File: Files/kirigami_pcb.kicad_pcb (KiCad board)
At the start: 2 copper layers, 67.7 x 70.4 mm, 24 parts, among them J1 In, J2 Thermistor, J3 Heater, J4 Fuse, J5 Fan, J6 Neopixel

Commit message: chain order
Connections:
- D1 pad 4: /DataOut -> Net-(D1-DIN)
- D8 pad 2: Net-(D8-DOUT) -> /DataIn
- J1 pad 3: Net-(D8-DOUT) -> /DataOut
- J1 pad 4: /DataIn -> Net-(D1-DIN)
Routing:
- net Net-(D8-DOUT): track 43.8 -> 0.00 mm, vias 1 -> 0
- net Net-(D1-DIN): track 0.00 -> 38.3 mm
- net /DataIn: track 21.1 -> 50.4 mm, vias 0 -> 1
- net /DataOut: track 20.9 -> 25.3 mm
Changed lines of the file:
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@@
   (net 15 "Net-(D6-DOUT)")
   (net 16 "Net-(D7-DOUT)")
-  (net 17 "Net-(D8-DOUT)")
+  (net 17 "Net-(D1-DIN)")
   (net 18 "Net-(D4-DOUT)")
   (net 19 "Net-(D5-DOUT)")
@@
       (net 10 "/Thermistor-Pad2") (pinfunction "Pin_2") (pintype "passive"))
     (pad "3" thru_hole circle (at 6 0 180) (size 1.5 1.5) (drill 1.02) (layers "*.Cu" "*.Mask")
-      (net 17 "Net-(D8-DOUT)") (pinfunction "Pin_3") (pintype "passive"))
+      (net 8 "/DataOut") (pinfunction "Pin_3") (pintype "passive"))
     (pad "4" thru_hole circle (at 9 0 180) (size 1.5 1.5) (drill 1.02) (layers "*.Cu" "*.Mask")
-      (net 7 "/DataIn") (pinfunction "Pin_4") (pintype "passive"))
+      (net 17 "Net-(D1-DIN)") (pinfunction "Pin_4") (pintype "passive"))
     (pad "5" thru_hole circle (at 12 0 180) (size 1.5 1.5) (drill 1.02) (layers "*.Cu" "*.Mask")
       (net 9 "/Neopixel5v") (pinfunction "Pin_5") (pintype "passive"))
@@
       (net 9 "/Neopixel5v") (pinfunction "VDD") (pintype "power_in"))
     (pad "2" smd rect (at -2.45 -1.65 200) (size 1.5 0.9) (layers "B.Cu" "B.Paste" "B.Mask")
-      (net 17 "Net-(D8-DOUT)") (pinfunction "DOUT") (pintype "output"))
+      (net 7 "/DataIn") (pinfunction "DOUT") (pintype "output"))
     (pad "3" smd rect (at 2.45 -1.65 200) (size 1.5 0.9) (layers "B.Cu" "B.Paste" "B.Mask")
       (net 6 "/NeopixelGND") (pinfunction "VSS") (pintype "power_in"))
@@
       (net 6 "/NeopixelGND") (pinfunction "VSS") (pintype "power_in"))
     (pad "4" smd rect (at 2.45 1.65 340) (size 1.5 0.9) (layers "B.Cu" "B.Paste" "B.Mask")
-      (net 8 "/DataOut") (pinfunction "DIN") (pintype "input"))
+      (net 17 "Net-(D1-DIN)") (pinfunction "DIN") (pintype "input"))
     (model "${KICAD6_3DMODEL_DIR}/LED_SMD.3dshapes/LED_WS2812B_PLCC4_5.0x5.0mm_P3.2mm.wrl"
       (offset (xyz 0 0 0))
@@
   (segment (start 199.025 67.175) (end 199.025 41.805645) (width 0.5) (layer "B.Cu") (net 6))
   (segment (start 180.875216 56.158867) (end 180.330141 56.158267) (width 0.5) (layer "B.Cu") (net 6))
-  (segment (start 203.8064 71.0036) (end 201.5011 71.0036) (width 0.5) (layer "B.Cu") (net 7))
-  (segment (start 211.1974 63.6126) (end 203.8064 71.0036) (width 0.5) (layer "B.Cu") (net 7))
-  (segment (start 219.0011 62.2336) (end 217.6221 63.6126) (width 0.5) (layer "B.Cu") (net 7))
-  (segment (start 217.6221 63.6126) (end 211.1974 63.6126) (width 0.5) (layer "B.Cu") (net 7))
-  (segment (start 203.95 75.95) (end 203.95 87.1) (width 0.5) (layer "B.Cu") (net 8))
-  (segment (start 201.60573 73.60573) (end 203.95 75.95) (width 0.5) (layer "B.Cu") (net 8))
-  (segment (start 199.684773 91.365227) (end 199.684773 91.790227) (width 0.5) (layer "B.Cu") (net 8))
-  (segment (start 203.95 87.1) (end 199.684773 91.365227) (width 0.5) (layer "B.Cu") (net 8))
+  (segment (start 205.8853 71) (end 201.5 71) (width 0.5) (layer "F.Cu") (net 7))
+  (segment (start 214.075 62.8103) (end 205.8853 71) (width 0.5) (layer "F.Cu") (net 7))
+  (segment (start 214.075 40.625) (end 214.075 62.8103) (width 0.5) (layer "F.Cu") (net 7))
+  (via (at 214.075 40.625) (size 0.6) (drill 0.3) (layers "F.Cu" "B.Cu") (net 7))
+  (segment (start 222.715254 31.984746) (end 214.075 40.625) (width 0.5) (layer "B.Cu") (net 7))
+  (segment (start 220.2 63.8) (end 222 62) (width 0.5) (layer "F.Cu") (net 8))
+  (segment (start 201.5 73.5) (end 205.9 73.5) (width 0.5) (layer "F.Cu") (net 8))
+  (segment (start 215.6 63.8) (end 220.2 63.8) (width 0.5) (layer "F.Cu") (net 8))
+  (segment (start 205.9 73.5) (end 215.6 63.8) (width 0.5) (layer "F.Cu") (net 8))
   (segment (start 208.5575 62) (end 208.0011 61.4436) (width 0.5) (layer "F.Cu") (net 9))
   (segment (start 210.4925 62) (end 208.5575 62) (width 0.5) (layer "F.Cu") (net 9))
@@
   (segment (start 200.472523 40.075) (end 207.514277 40.075) (width 0.5) (layer "B.Cu") (net 16))
   (segment (start 207.514277 40.075) (end 217.029617 30.55966) (width 0.5) (layer "B.Cu") (net 16))
-  (segment (start 219.8347 64.175) (end 222.0011 62.0086) (width 0.5) (layer "F.Cu") (net 17))
-  (segment (start 215.4397 64.175) (end 219.8347 64.175) (width 0.5) (layer "F.Cu") (net 17))
-  (segment (start 214.075 40.625) (end 214.075 62.8103) (width 0.5) (layer "F.Cu") (net 17))
-  (segment (start 214.075 62.8103) (end 215.4397 64.175) (width 0.5) (layer "F.Cu") (net 17))
-  (via (at 214.075 40.625) (size 0.6) (drill 0.3) (layers "F.Cu" "B.Cu") (net 17))
-  (segment (start 222.715254 31.984746) (end 214.075 40.625) (width 0.5) (layer "B.Cu") (net 17))
+  (segment (start 199.684773 91.365227) (end 199.684773 91.790227) (width 0.5) (layer "B.Cu") (net 17))
+  (segment (start 217.6221 63.6126) (end 216.2874 63.6126) (width 0.5) (layer "B.Cu") (net 17))
+  (segment (start 216.2874 63.6126) (end 203.95 75.95) (width 0.5) (layer "B.Cu") (net 17))
+  (segment (start 219.0011 62.2336) (end 217.6221 63.6126) (width 0.5) (layer "B.Cu") (net 17))
+  (segment (start 203.95 87.1) (end 199.684773 91.365227) (width 0.5) (layer "B.Cu") (net 17))
+  (segment (start 203.95 75.95) (end 203.95 87.1) (width 0.5) (layer "B.Cu") (net 17))
   (segment (start 182.42266 62.85234) (end 182.206476 63.068524) (width 0.5) (layer "B.Cu") (net 18))
   (segment (start 182.206476 63.068524) (end 177.842116 63.068524) (width 0.5) (layer "B.Cu") (net 18))

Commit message: Update kirigami_pcb.kicad_pcb
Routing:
- net /Fan-: track 22.6 -> 23.6 mm
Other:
- board text added: "V0 Kirigami PCB V2 U.F.O. Edition 8/8/23 L. Ries JLCJLCJLCJLC"
- board text removed: "V0 Kirigami PCB V2 - 10/16/22 L. Ries JLCJLCJLCJLC"

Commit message: Update kirigami_pcb.kicad_pcb
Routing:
- net /Neopixel5v: track 266.1 -> 202.0 mm
- net /NeopixelGND: track 196.5 -> 176.9 mm
- net Net-(D3-DOUT): track 19.2 -> 7.99 mm
- net Net-(D2-DOUT): track 9.49 -> 10.8 mm

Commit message: Update kirigami_pcb.kicad_pcb
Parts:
- moved C1 2.86 mm to (210.6, 60.0)
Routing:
- net /Neopixel5v: track 202.0 -> 197.1 mm
- net /NeopixelGND: track 176.9 -> 174.2 mm
- net /DataIn: track 50.4 -> 48.8 mm
- net /Fan-: track 23.6 -> 22.3 mm
- net Net-(D5-DOUT): track 13.3 -> 12.7 mm

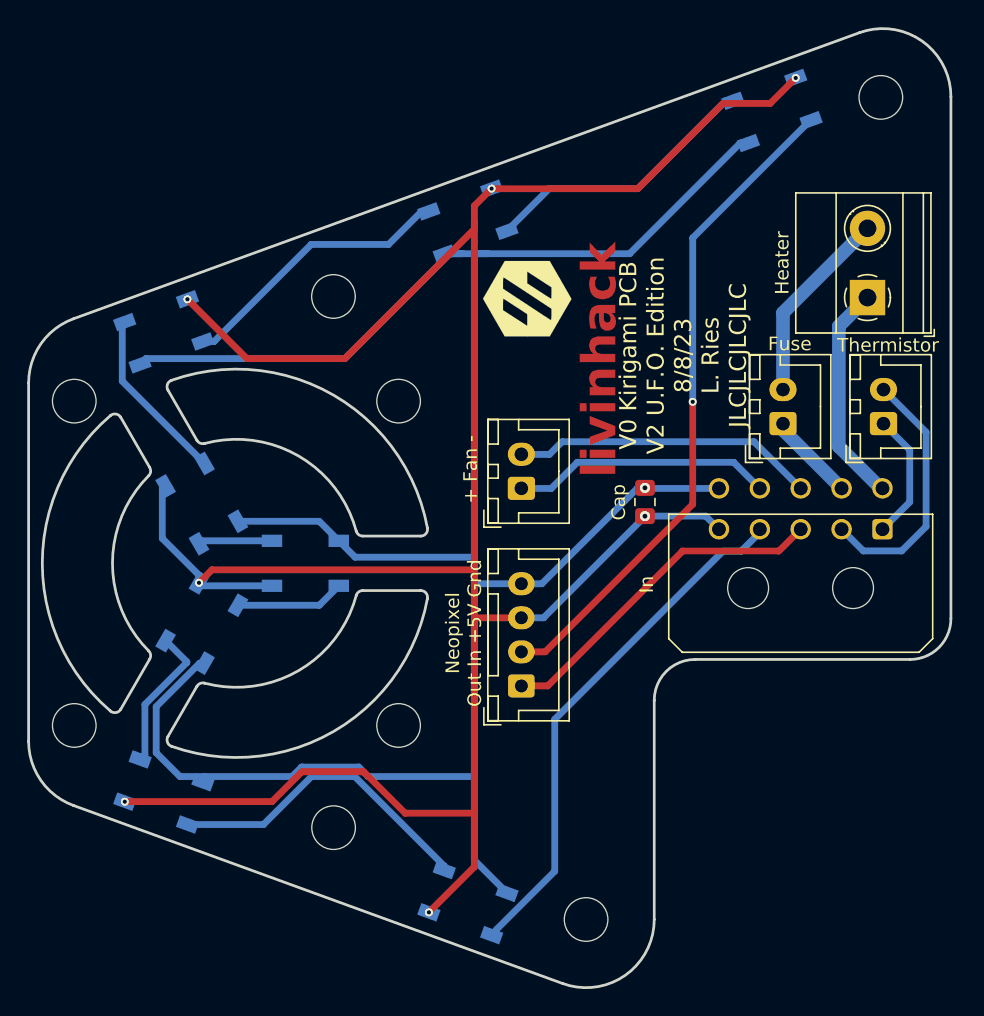
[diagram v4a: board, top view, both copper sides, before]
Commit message: round tracks
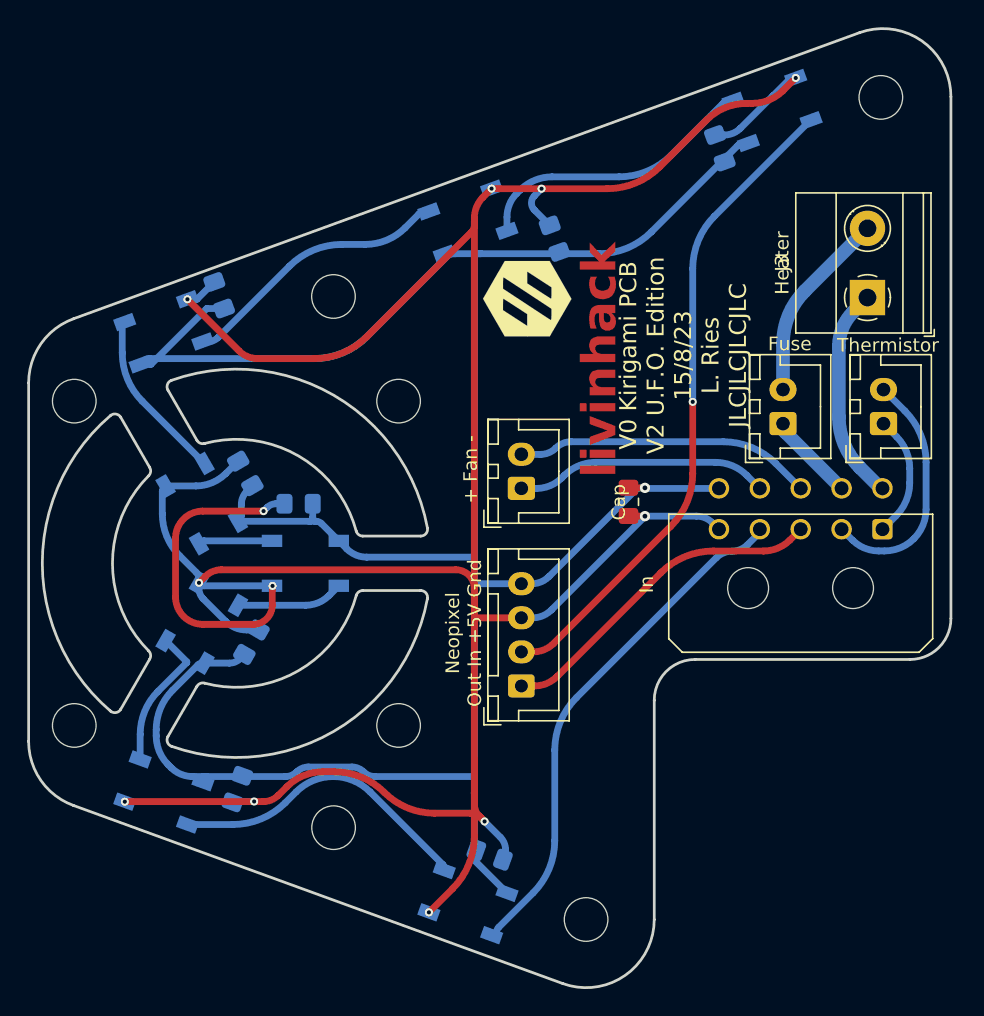
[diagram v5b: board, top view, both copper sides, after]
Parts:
- added C1: Cap, Capacitor_SMD:C_0805_2012Metric_Pad1.18x1.45mm_HandSolder, B.Cu at (199.2, 85.9)
- added C2: Cap, Capacitor_SMD:C_0805_2012Metric_Pad1.18x1.45mm_HandSolder, B.Cu at (180.7, 81.1)
- added C3: Cap, Capacitor_SMD:C_0805_2012Metric_Pad1.18x1.45mm_HandSolder, B.Cu at (181.7, 70.3)
- added C4: Cap, Capacitor_SMD:C_0805_2012Metric_Pad1.18x1.45mm_HandSolder, B.Cu at (185.2, 60.1)
- added C5: Cap, Capacitor_SMD:C_0805_2012Metric_Pad1.18x1.45mm_HandSolder, B.Cu at (181.2, 57.9)
- added C6: Cap, Capacitor_SMD:C_0805_2012Metric_Pad1.18x1.45mm_HandSolder, B.Cu at (179.3, 44.8)
- added C7: Cap, Capacitor_SMD:C_0805_2012Metric_Pad1.18x1.45mm_HandSolder, B.Cu at (203.9, 40.7)
- added C8: Cap, Capacitor_SMD:C_0805_2012Metric_Pad1.18x1.45mm_HandSolder, B.Cu at (216.1, 34.0)
- moved C9 1.21 mm to (209.4, 60.0), turned to -90 degrees
- renumbered C1 to C9
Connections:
- C9 pad 1: /Neopixel5v -> /NeopixelGND
- C9 pad 2: /NeopixelGND -> /Neopixel5v
- D1 pad 2: Net-(D1-DOUT) -> Dout>Din
- D1 pad 4: Net-(D1-DIN) -> /DataIn
- D2 pad 2: Net-(D2-DOUT) -> Dout>Din
- D2 pad 4: Net-(D1-DOUT) -> Dout>Din
- D3 pad 2: Net-(D3-DOUT) -> Dout>Din
- D3 pad 4: Net-(D2-DOUT) -> Dout>Din
- D4 pad 2: Net-(D4-DOUT) -> Dout>Din
- D4 pad 4: Net-(D3-DOUT) -> Dout>Din
- D5 pad 2: Net-(D5-DOUT) -> Dout>Din
- D5 pad 4: Net-(D4-DOUT) -> Dout>Din
- D6 pad 2: Net-(D6-DOUT) -> Dout>Din
- D6 pad 4: Net-(D5-DOUT) -> Dout>Din
- D7 pad 2: Net-(D7-DOUT) -> Dout>Din
- D7 pad 4: Net-(D6-DOUT) -> Dout>Din
- D8 pad 2: /DataIn -> Dout>Din
- D8 pad 4: Net-(D7-DOUT) -> Dout>Din
- J1 pad 4: Net-(D1-DIN) -> /DataIn
- J6 pad 2: /DataIn -> Dout>Din
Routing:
- net Dout>Din: track 0.00 -> 147.1 mm, vias 0 -> 1
- net /Neopixel5v: track 197.1 -> 252.8 mm, vias 7 -> 12
- net Net-(D1-DIN): track 38.3 -> 0.00 mm
- net Net-(D1-DOUT): track 23.3 -> 0.00 mm
- net Net-(D6-DOUT): track 20.5 -> 0.00 mm
- net Net-(D7-DOUT): track 20.1 -> 0.00 mm
- net /NeopixelGND: track 174.2 -> 187.8 mm
- net Net-(D5-DOUT): track 12.7 -> 0.00 mm
- net /DataIn: track 48.8 -> 37.6 mm, vias 1 -> 0
- net Net-(D2-DOUT): track 10.8 -> 0.00 mm
- net Net-(D3-DOUT): track 7.99 -> 0.00 mm
- net Net-(D4-DOUT): track 5.45 -> 0.00 mm
- net /Thermistor-Pad2: track 19.0 -> 18.3 mm
- net /DataOut: track 25.3 -> 24.8 mm
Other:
- board text added: "V0 Kirigami PCB V2 U.F.O. Edition 15/8/23 L. Ries JLCJLCJLCJLC"
- board text removed: "V0 Kirigami PCB V2 U.F.O. Edition 8/8/23 L. Ries JLCJLCJLCJLC"

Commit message: Update kirigami_pcb.kicad_pcb
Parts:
- moved C9 1.21 mm to (210.6, 60.0)
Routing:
- net /Neopixel5v: track 252.8 -> 256.1 mm
- net /NeopixelGND: track 187.8 -> 186.9 mm

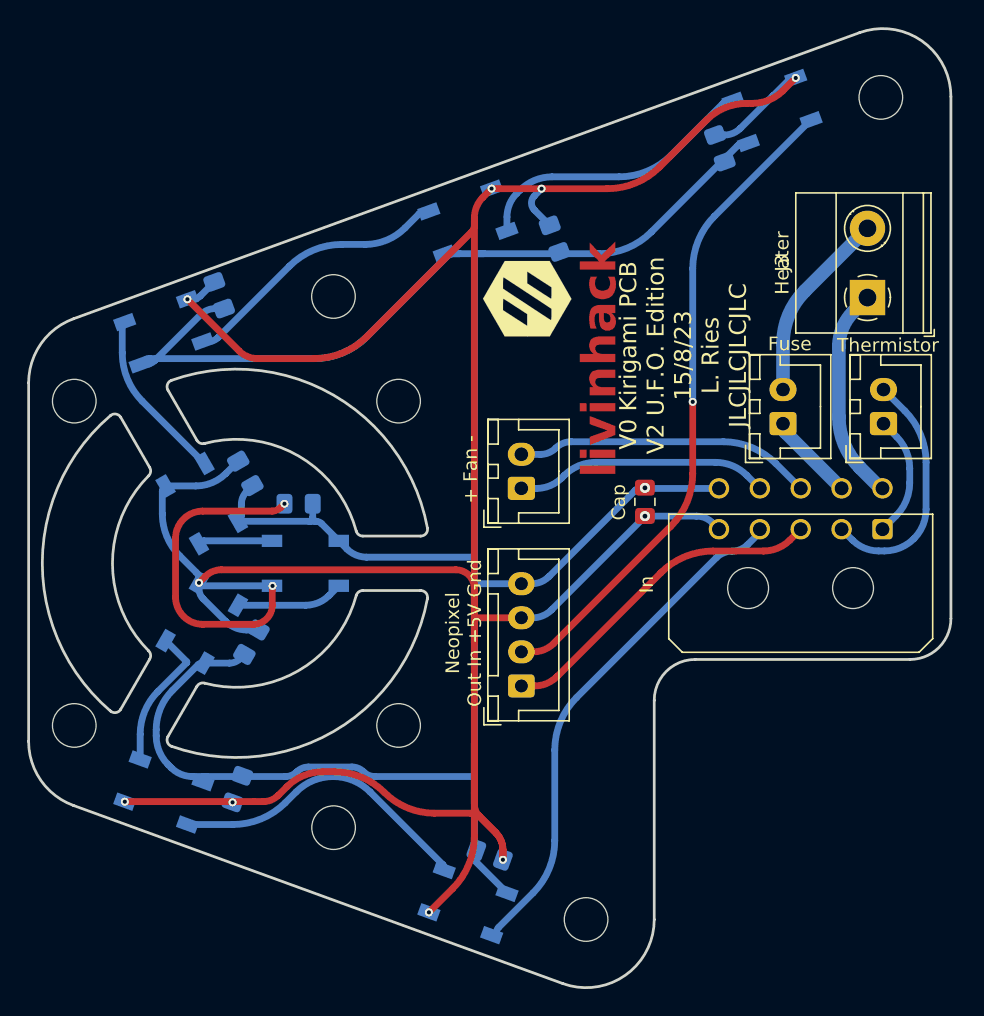
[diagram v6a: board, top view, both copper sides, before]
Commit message: Schematic cleanup and organization
A few changes to the schematic to aid in readability as well as simplifying signal flow.
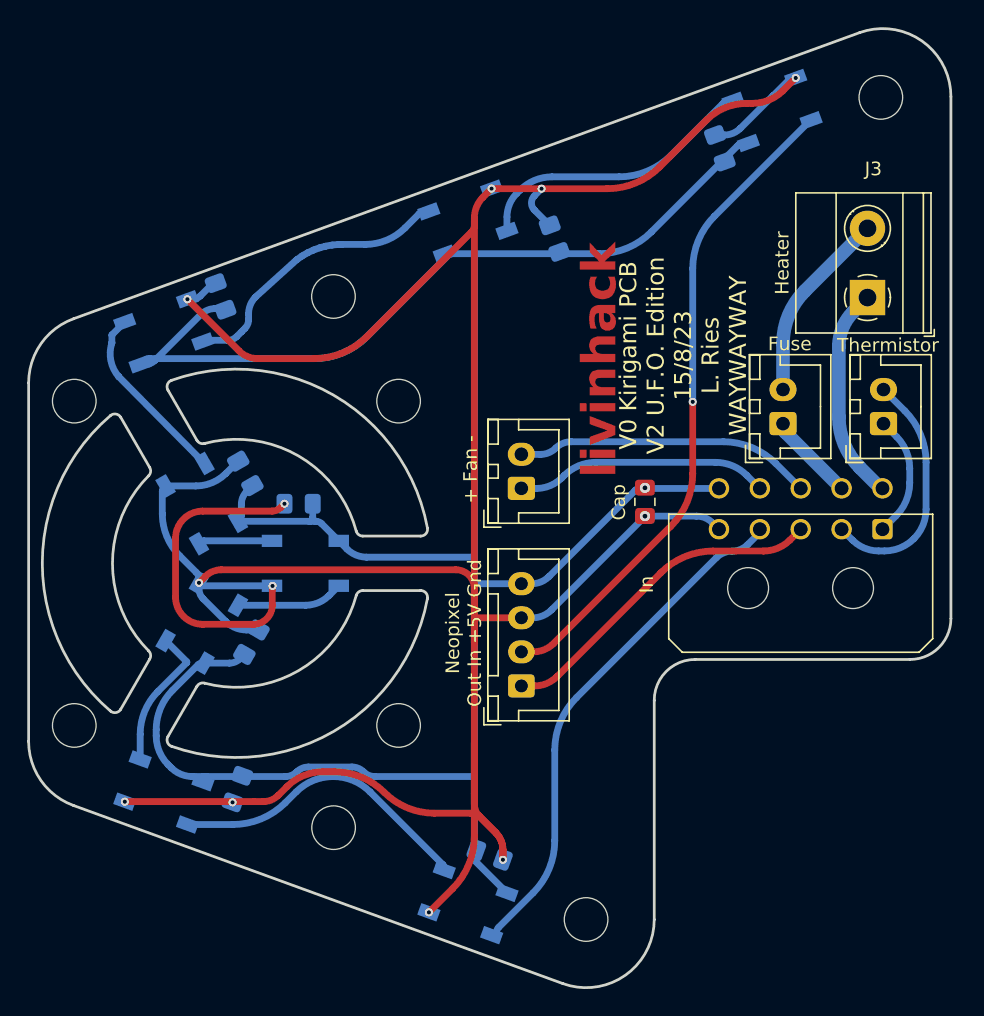
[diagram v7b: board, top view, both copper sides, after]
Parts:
- removed G***: LOGO, TRA_KiCad_Footprints:VoronLogo_6pt5mm_silkScreen
- J6: value Neopixel -> Front Neopixel
- moved C6 0.14 mm to (179.4, 44.9), turned to -70 degrees
- turned C1 to 160 degrees
- turned C2 to 70 degrees
- turned C3 to -120 degrees
- turned C4 to 0 degrees
- turned C5 to -60 degrees
- turned C7 to -70 degrees
- turned C8 to -70 degrees
- turned C9 to 90 degrees
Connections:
- net /DataIn renamed /Neo_In
- net /DataOut renamed /Neopixel Return
- C1 pad 1: /NeopixelGND -> /Neopixel5v
- C1 pad 2: /Neopixel5v -> /NeopixelGND
- C2 pad 1: /NeopixelGND -> /Neopixel5v
- C2 pad 2: /Neopixel5v -> /NeopixelGND
- C3 pad 1: /NeopixelGND -> /Neopixel5v
- C3 pad 2: /Neopixel5v -> /NeopixelGND
- C4 pad 1: /NeopixelGND -> /Neopixel5v
- C4 pad 2: /Neopixel5v -> /NeopixelGND
- C5 pad 1: /NeopixelGND -> /Neopixel5v
- C5 pad 2: /Neopixel5v -> /NeopixelGND
- C6 pad 1: /NeopixelGND -> /Neopixel5v
- C6 pad 2: /Neopixel5v -> /NeopixelGND
- C7 pad 1: /NeopixelGND -> /Neopixel5v
- C7 pad 2: /Neopixel5v -> /NeopixelGND
- C8 pad 1: /NeopixelGND -> /Neopixel5v
- C8 pad 2: /Neopixel5v -> /NeopixelGND
- C9 pad 1: /NeopixelGND -> /Neopixel5v
- C9 pad 2: /Neopixel5v -> /NeopixelGND
- D1 pad 2: Dout>Din -> Net-(D1-DOUT)
- D2 pad 2: Dout>Din -> Net-(D2-DOUT)
- D2 pad 4: Dout>Din -> Net-(D1-DOUT)
- D3 pad 2: Dout>Din -> Net-(D3-DOUT)
- D3 pad 4: Dout>Din -> Net-(D2-DOUT)
- D4 pad 2: Dout>Din -> Net-(D4-DOUT)
- D4 pad 4: Dout>Din -> Net-(D3-DOUT)
- D5 pad 2: Dout>Din -> Net-(D5-DOUT)
- D5 pad 4: Dout>Din -> Net-(D4-DOUT)
- D6 pad 2: Dout>Din -> Net-(D6-DOUT)
- D6 pad 4: Dout>Din -> Net-(D5-DOUT)
- D7 pad 2: Dout>Din -> Net-(D7-DOUT)
- D7 pad 4: Dout>Din -> Net-(D6-DOUT)
- D8 pad 2: Dout>Din -> /Neopixel Out
- D8 pad 4: Dout>Din -> Net-(D7-DOUT)
- J6 pad 2: Dout>Din -> /Neopixel Out
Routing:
- net Dout>Din: track 147.1 -> 0.00 mm, vias 1 -> 0
- net /Neopixel Out: track 0.00 -> 48.2 mm, vias 0 -> 1
- net Net-(D1-DOUT): track 0.00 -> 22.5 mm
- net Net-(D7-DOUT): track 0.00 -> 20.9 mm
- net Net-(D6-DOUT): track 0.00 -> 20.5 mm
- net Net-(D5-DOUT): track 0.00 -> 13.5 mm
- net Net-(D2-DOUT): track 0.00 -> 10.6 mm
- net Net-(D3-DOUT): track 0.00 -> 7.87 mm
- net Net-(D4-DOUT): track 0.00 -> 5.28 mm
- net /NeopixelGND: track 186.9 -> 185.1 mm
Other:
- board text added: "V0 Kirigami PCB V2 U.F.O. Edition 15/8/23 L. Ries WAYWAYWAY"
- board text removed: "V0 Kirigami PCB V2 U.F.O. Edition 15/8/23 L. Ries JLCJLCJLCJLC"
